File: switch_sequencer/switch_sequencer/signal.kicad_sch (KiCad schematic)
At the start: 9 parts, among them J8 3.5mm_Mono_Switched_sm, SW6 D6R90F2LFS, U10 TL072

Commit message: sequential switch wip more more
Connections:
- net GNDA is gone; now on net GND: J8.2 (SHEILD), J8.3 (SW), U10.5 (+)
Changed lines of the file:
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@@
+	)
+	(junction
+		(at 39.37 149.86)
+		(diameter 0)
+		(color 0 0 0 0)
 	)
 	(junction
 		(at 83.82 148.59)
-		(diameter 0)
-		(color 0 0 0 0)
-	)
-	(junction
-		(at 39.37 149.86)
 		(diameter 0)
 		(color 0 0 0 0)
@@
 			)
 			(justify right)
-		)
-	)
-	(symbol
-		(lib_id "4ms_Power-symbol:GNDA")
-		(at 93.98 161.29 180)
-		(unit 1)
-		(exclude_from_sim no)
-		(in_bom yes)
-		(on_board yes)
-		(dnp no)
-		(fields_autoplaced yes)
-		(property "Reference" "#PWR067"
-			(at 93.98 154.94 0)
-			(effects
-				(font
-					(size 1.27 1.27)
-				)
-				(hide yes)
-			)
-		)
-		(property "Value" "GNDA"
-			(at 93.98 156.21 0)
-			(effects
-				(font
-					(size 1.27 1.27)
-				)
-			)
-		)
-		(property "Footprint" ""
-			(at 93.98 161.29 0)
-			(effects
-				(font
-					(size 1.27 1.27)
-				)
-				(hide yes)
-			)
-		)
-		(property "Datasheet" ""
-			(at 93.98 161.29 0)
-			(effects
-				(font
-					(size 1.27 1.27)
-				)
-				(hide yes)
-			)
-		)
-		(property "Description" "(analog) ground power-flag symbol"
-			(at 93.98 161.29 0)
-			(effects
-				(font
-					(size 1.27 1.27)
-				)
-				(hide yes)
-			)
-		)
-		(pin "1"
-		)
-		(instances
-			(project "switch_sequencer"
-				(path "/1090b42d-0526-4901-ae26-1a4493d10820/4c22d006-f8e0-4fe5-9164-b59b12367ed8/3b32ef6f-f7de-4ddd-97a9-3d5452522cd1"
-					(reference "#PWR067")
-					(unit 1)
-				)
-				(path "/1090b42d-0526-4901-ae26-1a4493d10820/4c22d006-f8e0-4fe5-9164-b59b12367ed8/5043bc26-4ce4-47be-bac8-88b06297739f"
-					(reference "#PWR081")
-					(unit 1)
-				)
-				(path "/1090b42d-0526-4901-ae26-1a4493d10820/4c22d006-f8e0-4fe5-9164-b59b12367ed8/56a49501-ca12-4951-9aa9-3235726846b6"
-					(reference "#PWR034")
-					(unit 1)
-				)
-				(path "/1090b42d-0526-4901-ae26-1a4493d10820/4c22d006-f8e0-4fe5-9164-b59b12367ed8/7e64556a-f431-4fba-8c1d-6e9af7db61e9"
-					(reference "#PWR060")
-					(unit 1)
-				)
-				(path "/1090b42d-0526-4901-ae26-1a4493d10820/4c22d006-f8e0-4fe5-9164-b59b12367ed8/a947920c-59f2-438b-89ba-8e48f95d6dbc"
-					(reference "#PWR053")
-					(unit 1)
-				)
-				(path "/1090b42d-0526-4901-ae26-1a4493d10820/4c22d006-f8e0-4fe5-9164-b59b12367ed8/ab8d2706-56a5-4587-b9ef-c598dc5bc3f9"
-					(reference "#PWR010")
-					(unit 1)
-				)
-				(path "/1090b42d-0526-4901-ae26-1a4493d10820/4c22d006-f8e0-4fe5-9164-b59b12367ed8/f6bf03c5-1acc-4c33-9962-bfdc3f3d33ad"
-					(reference "#PWR017")
-					(unit 1)
-				)
-				(path "/1090b42d-0526-4901-ae26-1a4493d10820/4c22d006-f8e0-4fe5-9164-b59b12367ed8/ff53a658-11dc-478f-9769-67012b38ead8"
-					(reference "#PWR074")
-					(unit 1)
-				)
-			)
 		)
 	)
@@
 	)
 	(symbol
+		(lib_id "4ms_Power-symbol:GND")
+		(at 93.98 161.29 180)
+		(unit 1)
+		(exclude_from_sim no)
+		(in_bom yes)
+		(on_board yes)
+		(dnp no)
+		(property "Reference" "#PWR010"
+			(at 93.98 154.94 0)
+			(effects
+				(font
+					(size 1.27 1.27)
+				)
+				(hide yes)
+			)
+		)
+		(property "Value" "GND"
+			(at 93.98 157.48 0)
+			(effects
+				(font
+					(size 1.27 1.27)
+				)
+			)
+		)
+		(property "Footprint" ""
+			(at 93.98 161.29 0)
+			(effects
+				(font
+					(size 1.27 1.27)
+				)
+				(hide yes)
+			)
+		)
+		(property "Datasheet" ""
+			(at 93.98 161.29 0)
+			(effects
+				(font
+					(size 1.27 1.27)
+				)
+				(hide yes)
+			)
+		)
+		(property "Description" ""
+			(at 93.98 161.29 0)
+			(effects
+				(font
+					(size 1.27 1.27)
+				)
+				(hide yes)
+			)
+		)
+		(pin "1"
+		)
+		(instances
+			(project "switch_sequencer"
+				(path "/1090b42d-0526-4901-ae26-1a4493d10820/4c22d006-f8e0-4fe5-9164-b59b12367ed8/3b32ef6f-f7de-4ddd-97a9-3d5452522cd1"
+					(reference "#PWR067")
+					(unit 1)
+				)
+				(path "/1090b42d-0526-4901-ae26-1a4493d10820/4c22d006-f8e0-4fe5-9164-b59b12367ed8/5043bc26-4ce4-47be-bac8-88b06297739f"
+					(reference "#PWR081")
+					(unit 1)
+				)
+				(path "/1090b42d-0526-4901-ae26-1a4493d10820/4c22d006-f8e0-4fe5-9164-b59b12367ed8/56a49501-ca12-4951-9aa9-3235726846b6"
+					(reference "#PWR034")
+					(unit 1)
+				)
+				(path "/1090b42d-0526-4901-ae26-1a4493d10820/4c22d006-f8e0-4fe5-9164-b59b12367ed8/7e64556a-f431-4fba-8c1d-6e9af7db61e9"
+					(reference "#PWR060")
+					(unit 1)
+				)
+				(path "/1090b42d-0526-4901-ae26-1a4493d10820/4c22d006-f8e0-4fe5-9164-b59b12367ed8/a947920c-59f2-438b-89ba-8e48f95d6dbc"
+					(reference "#PWR053")
+					(unit 1)
+				)
+				(path "/1090b42d-0526-4901-ae26-1a4493d10820/4c22d006-f8e0-4fe5-9164-b59b12367ed8/ab8d2706-56a5-4587-b9ef-c598dc5bc3f9"
+					(reference "#PWR010")
+					(unit 1)
+				)
+				(path "/1090b42d-0526-4901-ae26-1a4493d10820/4c22d006-f8e0-4fe5-9164-b59b12367ed8/f6bf03c5-1acc-4c33-9962-bfdc3f3d33ad"
+					(reference "#PWR017")
+					(unit 1)
+				)
+				(path "/1090b42d-0526-4901-ae26-1a4493d10820/4c22d006-f8e0-4fe5-9164-b59b12367ed8/ff53a658-11dc-478f-9769-67012b38ead8"
+					(reference "#PWR074")
+					(unit 1)
+				)
+			)
+		)
+	)
+	(symbol
 		(lib_id "4ms_IC:TL072")
 		(at 101.6 166.37 0)
@@
 	)
 	(symbol
-		(lib_id "4ms_Power-symbol:GNDA")
-		(at 39.37 149.86 0)
-		(unit 1)
-		(exclude_from_sim no)
-		(in_bom yes)
-		(on_board yes)
-		(dnp no)
-		(fields_autoplaced yes)
-		(property "Reference" "#PWR063"
-			(at 39.37 156.21 0)
-			(effects
-				(font
-					(size 1.27 1.27)
-				)
-				(hide yes)
-			)
-		)
-		(property "Value" "GNDA"
-			(at 39.37 154.94 0)
-			(effects
-				(font
-					(size 1.27 1.27)
-				)
-			)
-		)
-		(property "Footprint" ""
-			(at 39.37 149.86 0)
-			(effects
-				(font
-					(size 1.27 1.27)
-				)
-				(hide yes)
-			)
-		)
-		(property "Datasheet" ""
-			(at 39.37 149.86 0)
-			(effects
-				(font
-					(size 1.27 1.27)
-				)
-				(hide yes)
-			)
-		)
-		(property "Description" "(analog) ground power-flag symbol"
-			(at 39.37 149.86 0)
-			(effects
-				(font
-					(size 1.27 1.27)
-				)
-				(hide yes)
-			)
-		)
-		(pin "1"
-		)
-		(instances
-			(project "switch_sequencer"
-				(path "/1090b42d-0526-4901-ae26-1a4493d10820/4c22d006-f8e0-4fe5-9164-b59b12367ed8/3b32ef6f-f7de-4ddd-97a9-3d5452522cd1"
-					(reference "#PWR063")
-					(unit 1)
-				)
-				(path "/1090b42d-0526-4901-ae26-1a4493d10820/4c22d006-f8e0-4fe5-9164-b59b12367ed8/5043bc26-4ce4-47be-bac8-88b06297739f"
-					(reference "#PWR077")
-					(unit 1)
-				)
-				(path "/1090b42d-0526-4901-ae26-1a4493d10820/4c22d006-f8e0-4fe5-9164-b59b12367ed8/56a49501-ca12-4951-9aa9-3235726846b6"
-					(reference "#PWR030")
-					(unit 1)
-				)
-				(path "/1090b42d-0526-4901-ae26-1a4493d10820/4c22d006-f8e0-4fe5-9164-b59b12367ed8/7e64556a-f431-4fba-8c1d-6e9af7db61e9"
-					(reference "#PWR056")
-					(unit 1)
-				)
-				(path "/1090b42d-0526-4901-ae26-1a4493d10820/4c22d006-f8e0-4fe5-9164-b59b12367ed8/a947920c-59f2-438b-89ba-8e48f95d6dbc"
-					(reference "#PWR037")
-					(unit 1)
-				)
-				(path "/1090b42d-0526-4901-ae26-1a4493d10820/4c22d006-f8e0-4fe5-9164-b59b12367ed8/ab8d2706-56a5-4587-b9ef-c598dc5bc3f9"
-					(reference "#PWR06")
-					(unit 1)
-				)
-				(path "/1090b42d-0526-4901-ae26-1a4493d10820/4c22d006-f8e0-4fe5-9164-b59b12367ed8/f6bf03c5-1acc-4c33-9962-bfdc3f3d33ad"
-					(reference "#PWR013")
-					(unit 1)
-				)
-				(path "/1090b42d-0526-4901-ae26-1a4493d10820/4c22d006-f8e0-4fe5-9164-b59b12367ed8/ff53a658-11dc-478f-9769-67012b38ead8"
-					(reference "#PWR070")
-					(unit 1)
-				)
-			)
-		)
-	)
-	(symbol
 		(lib_id "power:+12V")
 		(at 48.26 162.56 0)
@@
 					(unit 1)
 				)
+			)
+		)
+	)
+	(symbol
+		(lib_id "4ms_Power-symbol:GND")
+		(at 39.37 149.86 0)
+		(unit 1)
+		(exclude_from_sim no)
+		(in_bom yes)
+		(on_board yes)
+		(dnp no)
+		(property "Reference" "#PWR06"
+			(at 39.37 156.21 0)
+			(effects
+				(font
+					(size 1.27 1.27)
+				)
+				(hide yes)
+			)
+		)
+		(property "Value" "GND"
+			(at 39.37 153.67 0)
+			(effects
+				(font
+					(size 1.27 1.27)
+				)
+			)
+		)
+		(property "Footprint" ""
+			(at 39.37 149.86 0)
+			(effects
+				(font
+					(size 1.27 1.27)
+				)
+				(hide yes)
+			)
+		)
+		(property "Datasheet" ""
+			(at 39.37 149.86 0)
+			(effects
+				(font
+					(size 1.27 1.27)
+				)
+				(hide yes)
+			)
+		)
+		(property "Description" ""
+			(at 39.37 149.86 0)
+			(effects
+				(font
+					(size 1.27 1.27)
+				)
+				(hide yes)
+			)
+		)
+		(pin "1"
+		)
+		(instances
+			(project "switch_sequencer"
+				(path "/1090b42d-0526-4901-ae26-1a4493d10820/4c22d006-f8e0-4fe5-9164-b59b12367ed8/3b32ef6f-f7de-4ddd-97a9-3d5452522cd1"
+					(reference "#PWR063")
+					(unit 1)
+				)
+				(path "/1090b42d-0526-4901-ae26-1a4493d10820/4c22d006-f8e0-4fe5-9164-b59b12367ed8/5043bc26-4ce4-47be-bac8-88b06297739f"
+					(reference "#PWR077")
+					(unit 1)
+				)
+				(path "/1090b42d-0526-4901-ae26-1a4493d10820/4c22d006-f8e0-4fe5-9164-b59b12367ed8/56a49501-ca12-4951-9aa9-3235726846b6"
+					(reference "#PWR030")
+					(unit 1)
+				)
+				(path "/1090b42d-0526-4901-ae26-1a4493d10820/4c22d006-f8e0-4fe5-9164-b59b12367ed8/7e64556a-f431-4fba-8c1d-6e9af7db61e9"
+					(reference "#PWR056")
+					(unit 1)
+				)
+				(path "/1090b42d-0526-4901-ae26-1a4493d10820/4c22d006-f8e0-4fe5-9164-b59b12367ed8/a947920c-59f2-438b-89ba-8e48f95d6dbc"
+					(reference "#PWR037")
+					(unit 1)
+				)
+				(path "/1090b42d-0526-4901-ae26-1a4493d10820/4c22d006-f8e0-4fe5-9164-b59b12367ed8/ab8d2706-56a5-4587-b9ef-c598dc5bc3f9"
+					(reference "#PWR06")
+					(unit 1)
+				)
+				(path "/1090b42d-0526-4901-ae26-1a4493d10820/4c22d006-f8e0-4fe5-9164-b59b12367ed8/f6bf03c5-1acc-4c33-9962-bfdc3f3d33ad"
+					(reference "#PWR013")
+					(unit 1)
+				)
+				(path "/1090b42d-0526-4901-ae26-1a4493d10820/4c22d006-f8e0-4fe5-9164-b59b12367ed8/ff53a658-11dc-478f-9769-67012b38ead8"
+					(reference "#PWR070")
+					(unit 1)
+				)

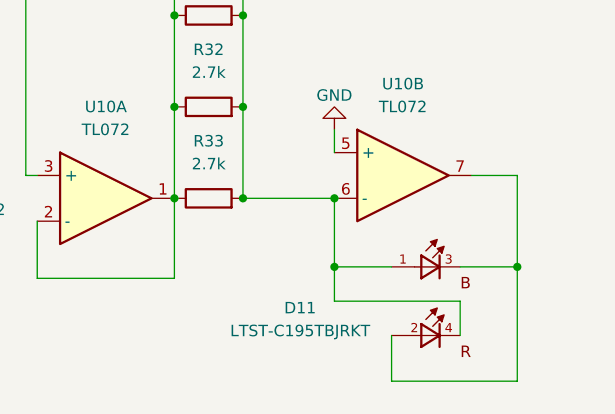
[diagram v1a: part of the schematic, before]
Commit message: sequential switch finished
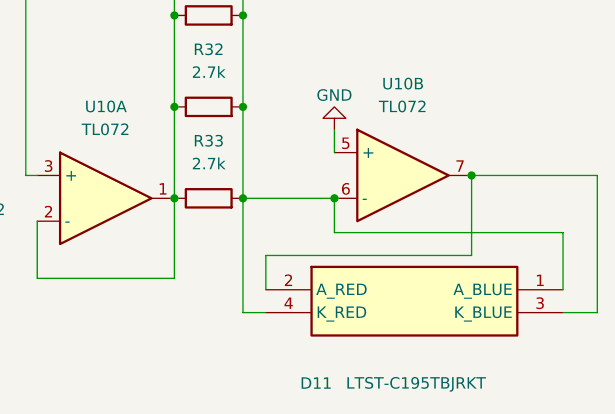
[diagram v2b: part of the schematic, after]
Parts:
- D11: footprint LTST-C195TBJRKT:LED_LTST-C195TBJRKT -> SamacSys_Parts:LTSTC195TBJRKT; symbol LTST-C195TBJRKT:LTST-C195TBJRKT -> SamacSys_Parts:LTST-C195TBJRKT; Height (none) -> 0.65; Manufacturer_Name (none) -> Lite-On; Manufacturer_Part_Number (none) -> LTST-C195TBJRKT; Mouser Part Number (none) -> 859-LTST-C195TBJRKT; Mouser Price/Stock (none) -> https://www.mouser.co.uk/ProductDetail/Lite-On/LTST-C195TBJ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
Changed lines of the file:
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@@
 	(paper "A4")
-	(junction
-		(at 114.3 176.53)
-		(diameter 0)
-		(color 0 0 0 0)
-	)
 	(junction
 		(at 39.37 149.86)
@@
 	)
 	(junction
-		(at 93.98 168.91)
-		(diameter 0)
-		(color 0 0 0 0)
-	)
-	(junction
-		(at 93.98 176.53)
-		(diameter 0)
-		(color 0 0 0 0)
-	)
-	(junction
 		(at 59.69 139.7)
 		(diameter 0)
@@
 	)
 	(junction
+		(at 93.98 168.91)
+		(diameter 0)
+		(color 0 0 0 0)
+	)
+	(junction
 		(at 76.2 148.59)
 		(diameter 0)
 		(color 0 0 0 0)
 	)
-	(wire
-		(pts
-			(xy 114.3 166.37) (xy 109.22 166.37)
+	(junction
+		(at 109.22 166.37)
+		(diameter 0)
+		(color 0 0 0 0)
+	)
+	(wire
+		(pts
+			(xy 109.22 166.37) (xy 123.19 166.37)
 		)
 		(stroke
@@
 	(wire
 		(pts
+			(xy 119.38 179.07) (xy 119.38 172.72)
+		)
+		(stroke
+			(width 0)
+			(type default)
+		)
+	)
+	(wire
+		(pts
 			(xy 76.2 177.8) (xy 76.2 168.91)
 		)
@@
 	(wire
 		(pts
-			(xy 107.95 180.34) (xy 107.95 184.15)
-		)
-		(stroke
-			(width 0)
-			(type default)
-		)
-	)
-	(wire
-		(pts
-			(xy 93.98 176.53) (xy 93.98 168.91)
+			(xy 93.98 172.72) (xy 93.98 168.91)
 		)
 		(stroke
@@
 	(wire
 		(pts
-			(xy 114.3 176.53) (xy 114.3 166.37)
-		)
-		(stroke
-			(width 0)
-			(type default)
-		)
-	)
-	(wire
-		(pts
 			(xy 45.72 149.86) (xy 39.37 149.86)
 		)
@@
 	(wire
 		(pts
-			(xy 93.98 176.53) (xy 93.98 180.34)
+			(xy 86.36 179.07) (xy 86.36 175.26)
+		)
+		(stroke
+			(width 0)
+			(type default)
+		)
+	)
+	(wire
+		(pts
+			(xy 119.38 172.72) (xy 93.98 172.72)
 		)
 		(stroke
@@
 	(wire
 		(pts
-			(xy 100.33 176.53) (xy 93.98 176.53)
-		)
-		(stroke
-			(width 0)
-			(type default)
-		)
-	)
-	(wire
-		(pts
-			(xy 114.3 176.53) (xy 107.95 176.53)
-		)
-		(stroke
-			(width 0)
-			(type default)
-		)
-	)
-	(wire
-		(pts
 			(xy 76.2 138.43) (xy 76.2 148.59)
 		)
@@
 	(wire
 		(pts
-			(xy 100.33 184.15) (xy 100.33 189.23)
-		)
-		(stroke
-			(width 0)
-			(type default)
-		)
-	)
-	(wire
-		(pts
-			(xy 100.33 189.23) (xy 114.3 189.23)
-		)
-		(stroke
-			(width 0)
-			(type default)
-		)
-	)
-	(wire
-		(pts
-			(xy 93.98 180.34) (xy 107.95 180.34)
+			(xy 109.22 175.26) (xy 109.22 166.37)
+		)
+		(stroke
+			(width 0)
+			(type default)
+		)
+	)
+	(wire
+		(pts
+			(xy 119.38 181.61) (xy 123.19 181.61)
+		)
+		(stroke
+			(width 0)
+			(type default)
+		)
+	)
+	(wire
+		(pts
+			(xy 86.36 181.61) (xy 83.82 181.61)
 		)
 		(stroke
@@
 	(wire
 		(pts
-			(xy 114.3 189.23) (xy 114.3 176.53)
-		)
-		(stroke
-			(width 0)
-			(type default)
-		)
-	)
-	(wire
-		(pts
 			(xy 76.2 158.75) (xy 76.2 168.91)
 		)
@@
 	(wire
 		(pts
+			(xy 123.19 181.61) (xy 123.19 166.37)
+		)
+		(stroke
+			(width 0)
+			(type default)
+		)
+	)
+	(wire
+		(pts
+			(xy 83.82 168.91) (xy 83.82 181.61)
+		)
+		(stroke
+			(width 0)
+			(type default)
+		)
+	)
+	(wire
+		(pts
 			(xy 83.82 148.59) (xy 83.82 158.75)
 		)
@@
 		(pts
 			(xy 60.96 177.8) (xy 76.2 177.8)
+		)
+		(stroke
+			(width 0)
+			(type default)
+		)
+	)
+	(wire
+		(pts
+			(xy 86.36 175.26) (xy 109.22 175.26)
 		)
 		(stroke
@@
 	)
 	(symbol
-		(lib_id "LTST-C195TBJRKT:LTST-C195TBJRKT")
-		(at 102.87 181.61 0)
+		(lib_id "SamacSys_Parts:LTST-C195TBJRKT")
+		(at 86.36 179.07 0)
 		(unit 1)
 		(exclude_from_sim no)
@@
 		(dnp no)
 		(property "Reference" "D11"
-			(at 90.17 181.102 0)
+			(at 91.948 189.484 0)
 			(effects
 				(font
@@
 		)
 		(property "Value" "LTST-C195TBJRKT"
-			(at 90.17 183.642 0)
-			(effects
-				(font
-					(size 1.27 1.27)
-				)
-			)
-		)
-		(property "Footprint" "LTST-C195TBJRKT:LED_LTST-C195TBJRKT"
-			(at 102.87 181.61 0)
+			(at 95.25 188.722 0)
+			(effects
+				(font
+					(size 1.27 1.27)
+				)
+				(justify left top)
+			)
+		)
+		(property "Footprint" "SamacSys_Parts:LTSTC195TBJRKT"
+			(at 115.57 273.99 0)
+			(effects
+				(font
+					(size 1.27 1.27)
+				)
+				(justify left top)
+				(hide yes)
+			)
+		)
+		(property "Datasheet" "https://optoelectronics.liteon.com/upload/download/DS22-2001-079/LTST-C195TBJRKT%20.pdf"
+			(at 115.57 373.99 0)
+			(effects
+				(font
+					(size 1.27 1.27)
+				)
+				(justify left top)
+				(hide yes)
+			)
+		)
+		(property "Description" "LED,SMD,0605,Bi-Colour,Blue/Red Lite-On LTST-C195TBJRKT Bi-colour Blue, Red LED, 470 / 631 nm, 4-Pin 1513 (0605), Rectangle Lens SMD Package"
+			(at 86.36 179.07 0)
+			(effects
+				(font
+					(size 1.27 1.27)
+				)
+				(hide yes)
+			)
+		)
+		(property "PARTREV" ""
+			(at 86.36 179.07 0)
 			(effects
 				(font
@@
 			)
 		)
-		(property "Datasheet" ""
-			(at 102.87 181.61 0)
-			(effects
-				(font
-					(size 1.27 1.27)
-				)
-				(hide yes)
-			)
-		)
-		(property "Description" ""
-			(at 102.87 181.61 0)
-			(effects
-				(font
-					(size 1.27 1.27)
-				)
-				(hide yes)
-			)
-		)
-		(property "PARTREV" ""
-			(at 102.87 181.61 0)
+		(property "MANUFACTURER" "Lite-On Inc."
+			(at 86.36 179.07 0)
 			(effects
 				(font
@@
 			)
 		)
-		(property "MANUFACTURER" "Lite-On Inc."
-			(at 102.87 181.61 0)
+		(property "STANDARD" "Manufacturer Recommendation"
+			(at 86.36 179.07 0)
 			(effects
 				(font
@@
 			)
 		)
-		(property "STANDARD" "Manufacturer Recommendation"
-			(at 102.87 181.61 0)
-			(effects
-				(font
-					(size 1.27 1.27)
-				)
-				(justify bottom)
+		(property "Height" "0.65"
+			(at 115.57 573.99 0)
+			(effects
+				(font
+					(size 1.27 1.27)
+				)
+				(justify left top)
+				(hide yes)
+			)
+		)
+		(property "Mouser Part Number" "859-LTST-C195TBJRKT"
+			(at 115.57 673.99 0)
+			(effects
+				(font
+					(size 1.27 1.27)
+				)
+				(justify left top)
+				(hide yes)
+			)
+		)
+		(property "Mouser Price/Stock" "https://www.mouser.co.uk/ProductDetail/Lite-On/LTST-C195TBJRKT?qs=zkxzjn%2FNGl5uy8%252BmRt4Q0Q%3D%3D"
+			(at 115.57 773.99 0)
+			(effects
+				(font
+					(size 1.27 1.27)
+				)
+				(justify left top)
+				(hide yes)
+			)
+		)
+		(property "Manufacturer_Name" "Lite-On"
+			(at 115.57 873.99 0)
+			(effects
+				(font
+					(size 1.27 1.27)
+				)
+				(justify left top)
+				(hide yes)
+			)
+		)
+		(property "Manufacturer_Part_Number" "LTST-C195TBJRKT"
+			(at 115.57 973.99 0)
+			(effects
+				(font
+					(size 1.27 1.27)
+				)
+				(justify left top)
 				(hide yes)
 			)
@@
 		(on_board yes)
 		(dnp no)
-		(property "Reference" "#PWR010"
+		(property "Reference" "#PWR067"
 			(at 93.98 154.94 0)
 			(effects
@@
 		(on_board yes)
 		(dnp no)
-		(property "Reference" "#PWR06"
+		(property "Reference" "#PWR063"
 			(at 39.37 156.21 0)
 			(effects
